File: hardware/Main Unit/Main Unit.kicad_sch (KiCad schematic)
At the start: 2 parts

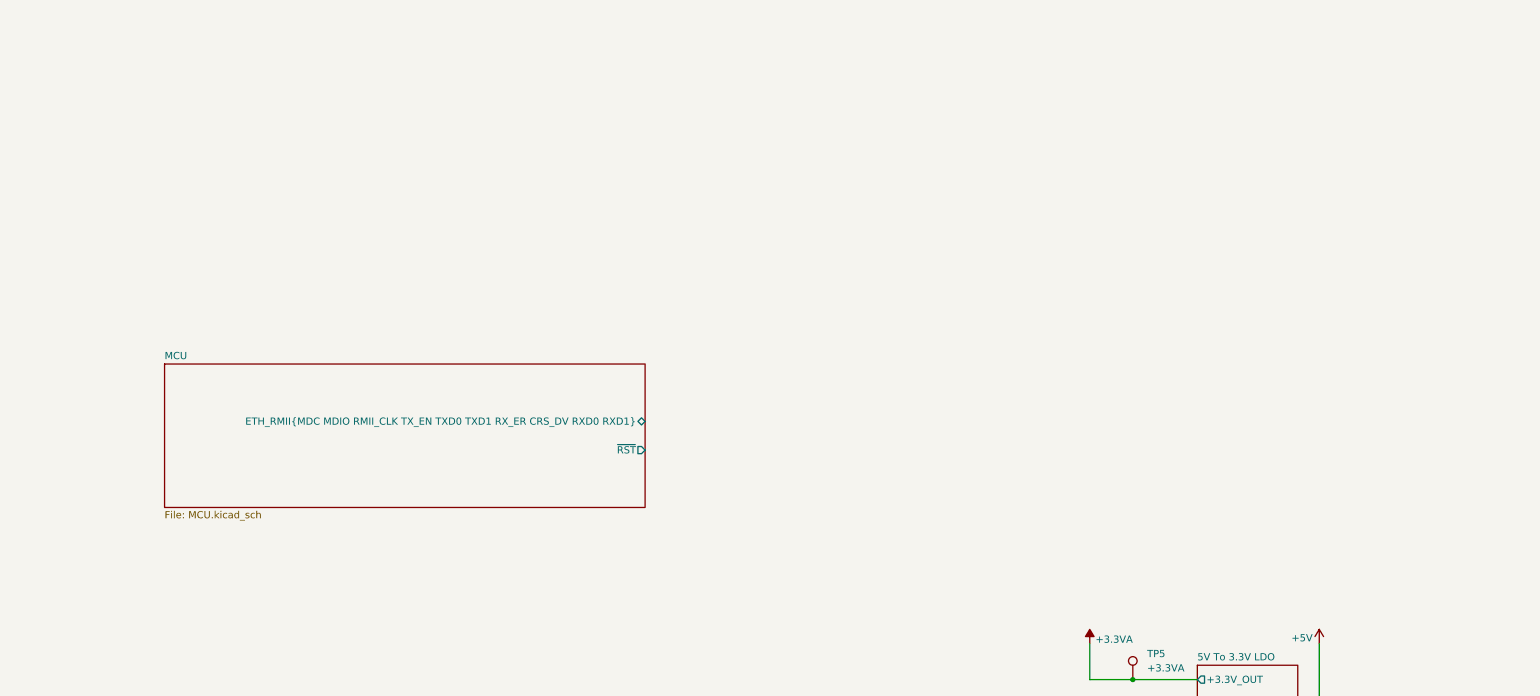
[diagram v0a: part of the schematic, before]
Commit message: Implement card connector schematic
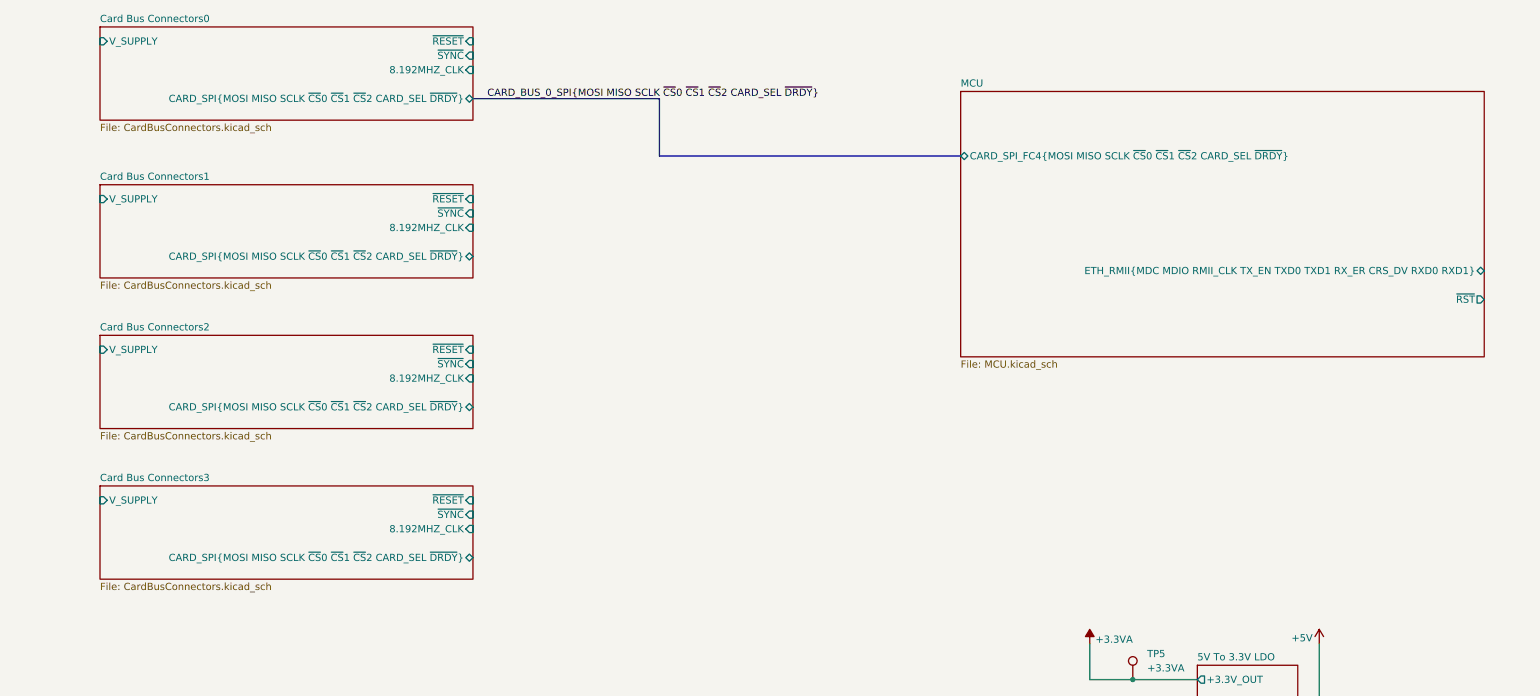
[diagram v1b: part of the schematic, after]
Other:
- added sheet Card Bus Connectors0 (CardBusConnectors.kicad_sch)
- added sheet Card Bus Connectors1 (CardBusConnectors.kicad_sch)
- added sheet Card Bus Connectors2 (CardBusConnectors.kicad_sch)
- added sheet Card Bus Connectors3 (CardBusConnectors.kicad_sch)
- sheet MCU ports: added CARD_SPI_FC4{MOSI MISO SCLK ~{CS}0 ~{CS}1 ~{CS}2 CARD_SEL ~{DRDY}}; removed none

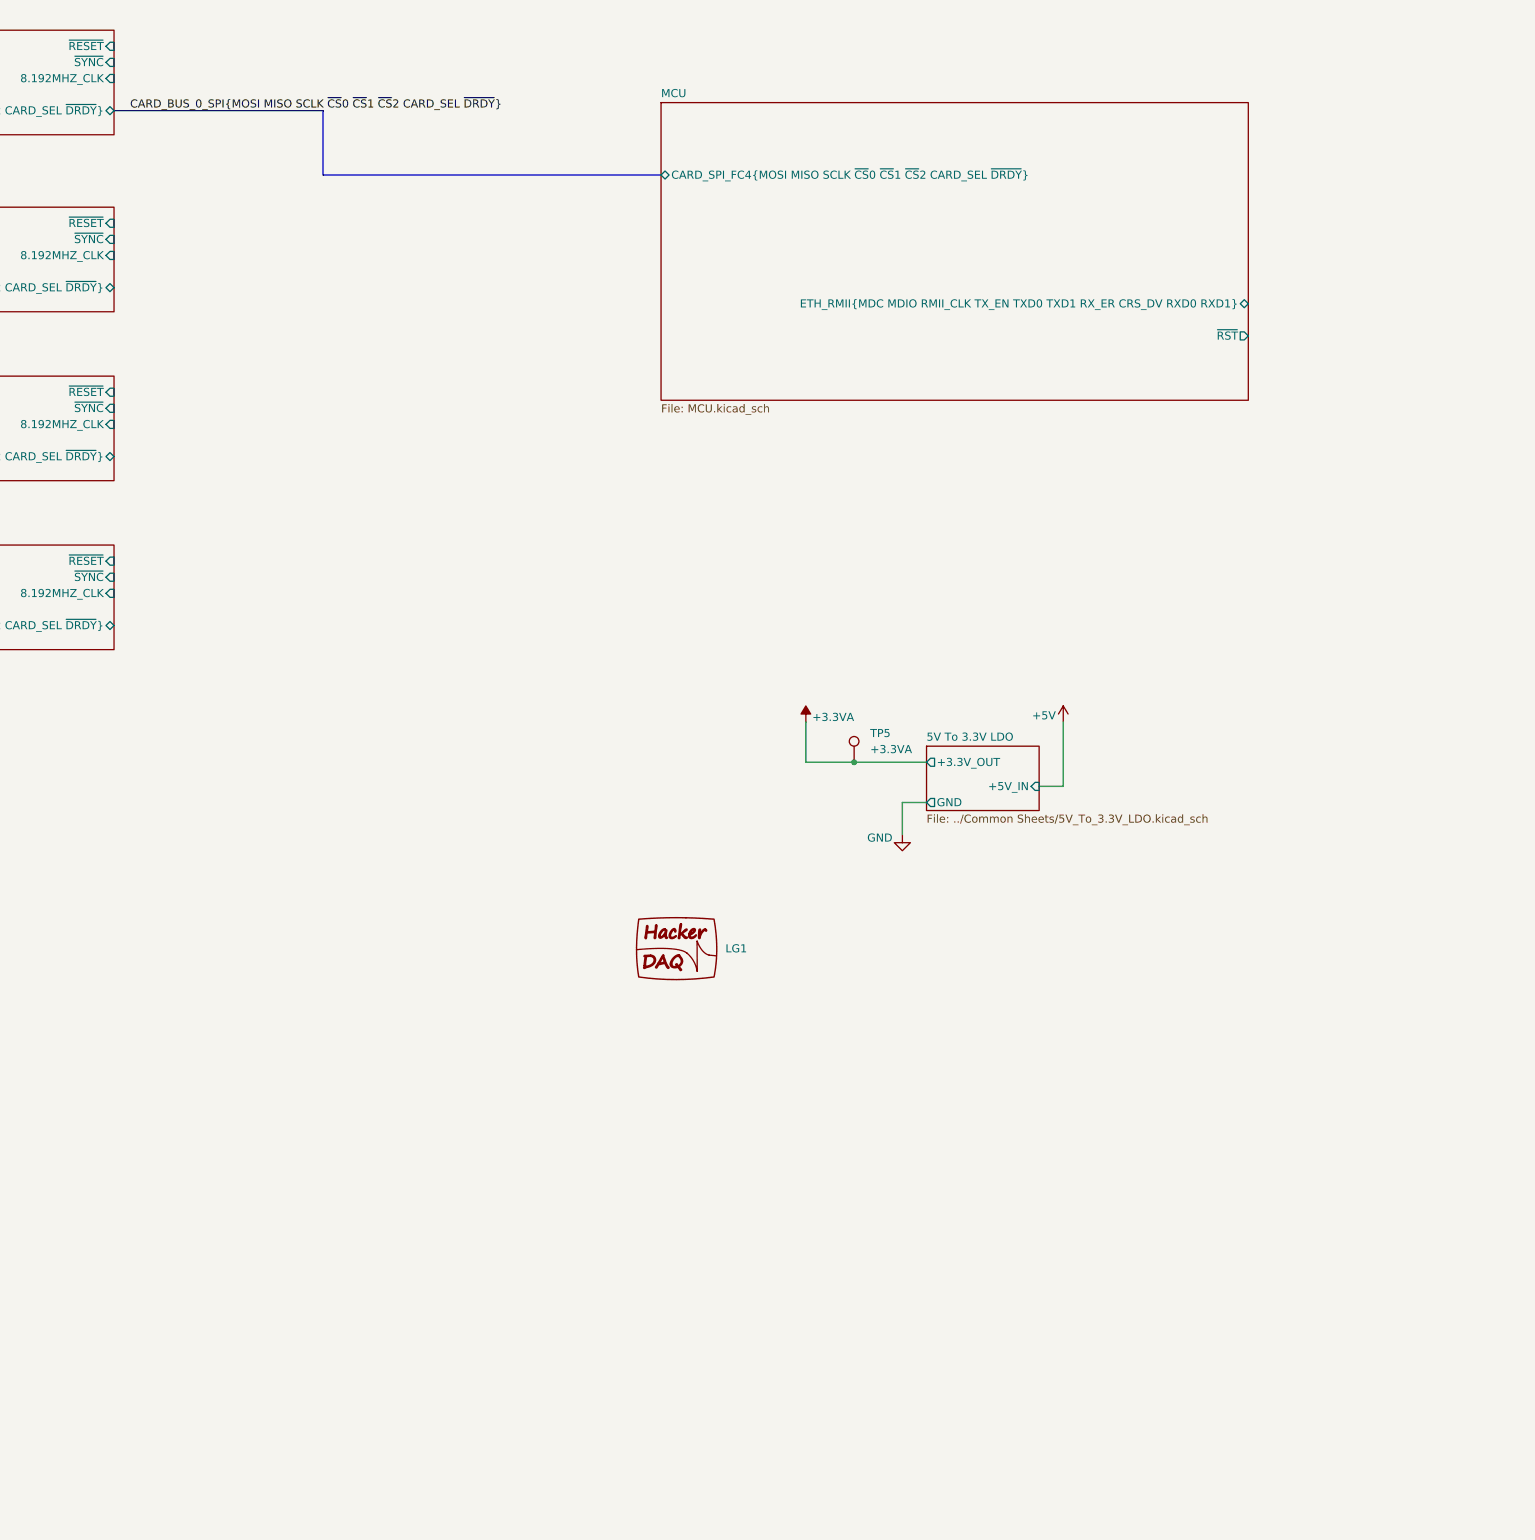
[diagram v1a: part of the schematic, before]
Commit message: Add MicroSD card, finish MCU symbol
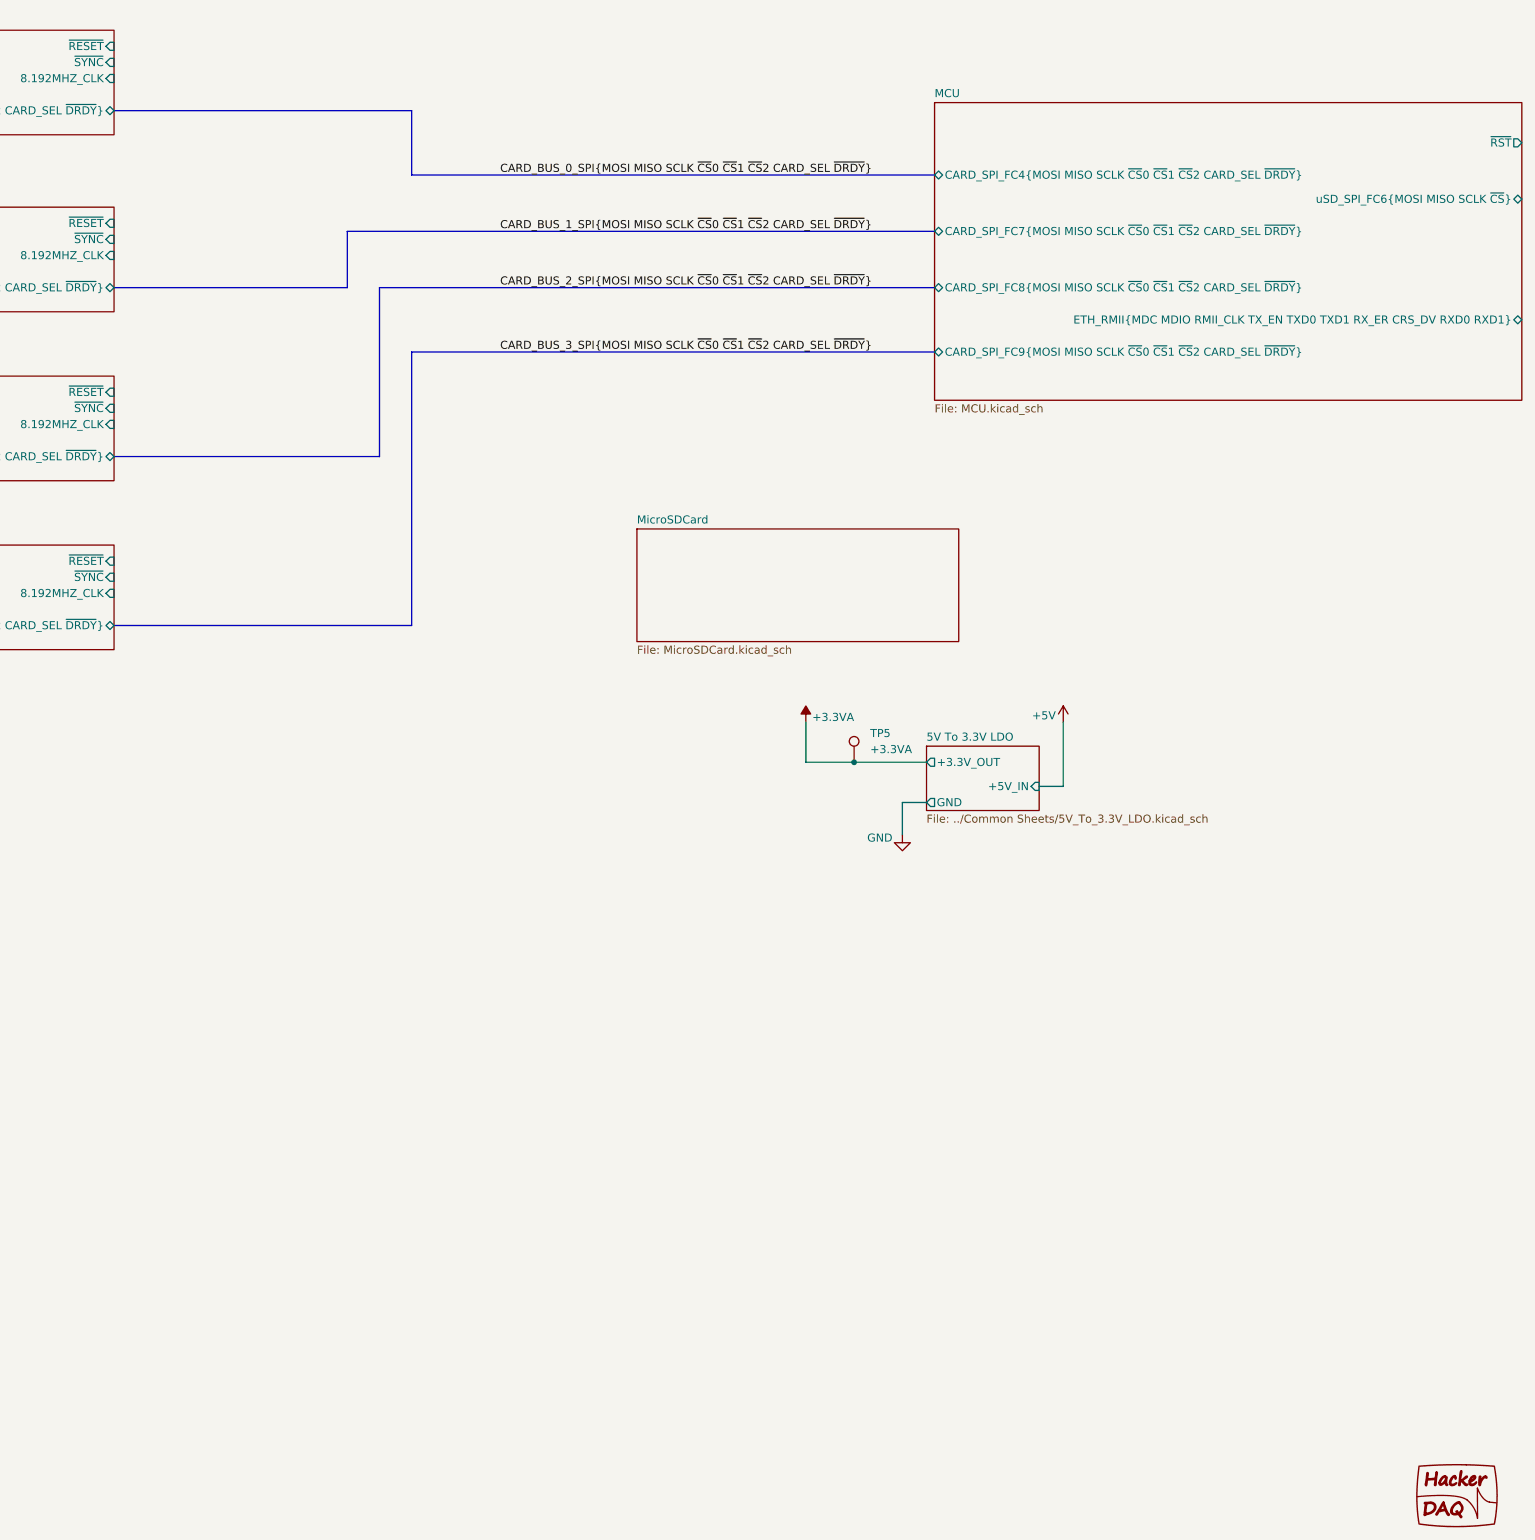
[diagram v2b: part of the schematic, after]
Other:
- added sheet MicroSDCard (MicroSDCard.kicad_sch)
- sheet MCU ports: added CARD_SPI_FC7{MOSI MISO SCLK ~{CS}0 ~{CS}1 ~{CS}2 CARD_SEL ~{DRDY}}, CARD_SPI_FC8{MOSI MISO SCLK ~{CS}0 ~{CS}1 ~{CS}2 CARD_SEL ~{DRDY}}, CARD_SPI_FC9{MOSI MISO SCLK ~{CS}0 ~{CS}1 ~{CS}2 CARD_SEL ~{DRDY}}, uSD_SPI_FC6{MOSI MISO SCLK ~{CS}}; removed none
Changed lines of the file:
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@@
 	(generator "eeschema")
 	(generator_version "9.0")
-	(paper "A4")
+	(paper "A3")
 	(junction
 		(at 213.36 144.78)
@@
 		(color 0 0 0 0)
 	)
+	(bus
+		(pts
+			(xy 138.43 69.85) (xy 226.06 69.85)
+		)
+		(stroke
+			(width 0)
+			(type default)
+		)
+	)
 	(wire
 		(pts
@@
 	(bus
 		(pts
-			(xy 129.54 52.07) (xy 129.54 41.91)
+			(xy 143.51 52.07) (xy 143.51 41.91)
 		)
 		(stroke
@@
 		)
 	)
+	(bus
+		(pts
+			(xy 133.35 60.96) (xy 133.35 69.85)
+		)
+		(stroke
+			(width 0)
+			(type default)
+		)
+	)
+	(bus
+		(pts
+			(xy 138.43 96.52) (xy 96.52 96.52)
+		)
+		(stroke
+			(width 0)
+			(type default)
+		)
+	)
+	(bus
+		(pts
+			(xy 143.51 123.19) (xy 96.52 123.19)
+		)
+		(stroke
+			(width 0)
+			(type default)
+		)
+	)
+	(bus
+		(pts
+			(xy 138.43 69.85) (xy 138.43 96.52)
+		)
+		(stroke
+			(width 0)
+			(type default)
+		)
+	)
+	(bus
+		(pts
+			(xy 143.51 80.01) (xy 143.51 123.19)
+		)
+		(stroke
+			(width 0)
+			(type default)
+		)
+	)
+	(bus
+		(pts
+			(xy 143.51 80.01) (xy 226.06 80.01)
+		)
+		(stroke
+			(width 0)
+			(type default)
+		)
+	)
 	(wire
 		(pts
@@
 	(bus
 		(pts
-			(xy 96.52 41.91) (xy 129.54 41.91)
+			(xy 96.52 41.91) (xy 143.51 41.91)
 		)
 		(stroke
@@
 	(bus
 		(pts
-			(xy 129.54 52.07) (xy 182.88 52.07)
+			(xy 143.51 52.07) (xy 226.06 52.07)
+		)
+		(stroke
+			(width 0)
+			(type default)
+		)
+	)
+	(bus
+		(pts
+			(xy 133.35 60.96) (xy 226.06 60.96)
+		)
+		(stroke
+			(width 0)
+			(type default)
+		)
+	)
+	(bus
+		(pts
+			(xy 133.35 69.85) (xy 96.52 69.85)
 		)
 		(stroke
@@
 	)
 	(label "CARD_BUS_0_SPI{MOSI MISO SCLK ~{CS}0 ~{CS}1 ~{CS}2 CARD_SEL ~{DRDY}}"
-		(at 99.06 41.91 0)
+		(at 157.48 52.07 0)
+		(effects
+			(font
+				(size 1.27 1.27)
+			)
+			(justify left bottom)
+		)
+	)
+	(label "CARD_BUS_2_SPI{MOSI MISO SCLK ~{CS}0 ~{CS}1 ~{CS}2 CARD_SEL ~{DRDY}}"
+		(at 157.48 69.85 0)
+		(effects
+			(font
+				(size 1.27 1.27)
+			)
+			(justify left bottom)
+		)
+	)
+	(label "CARD_BUS_3_SPI{MOSI MISO SCLK ~{CS}0 ~{CS}1 ~{CS}2 CARD_SEL ~{DRDY}}"
+		(at 157.48 80.01 0)
+		(effects
+			(font
+				(size 1.27 1.27)
+			)
+			(justify left bottom)
+		)
+	)
+	(label "CARD_BUS_1_SPI{MOSI MISO SCLK ~{CS}0 ~{CS}1 ~{CS}2 CARD_SEL ~{DRDY}}"
+		(at 157.48 60.96 0)
 		(effects
 			(font
@@
 	(symbol
 		(lib_id "Project Library:HackerDAQ_Logo")
-		(at 182.88 170.18 0)
+		(at 306.07 256.54 0)
 		(unit 1)
 		(exclude_from_sim no)
@@
 		(fields_autoplaced yes)
 		(property "Reference" "LG1"
-			(at 193.04 174.2016 0)
-			(effects
-				(font
-					(size 1.27 1.27)
-				)
-				(justify left)
+			(at 316.23 260.5616 0)
+			(effects
+				(font
+					(size 1.27 1.27)
+				)
+				(justify left)
+				(hide yes)
 			)
 		)
 		(property "Value" "~"
-			(at 182.88 170.18 0)
+			(at 306.07 256.54 0)
 			(effects
 				(font
@@
 		)
 		(property "Footprint" "Project Library:HackerDAQ Logo"
-			(at 194.056 165.1 0)
+			(at 317.246 251.46 0)
 			(effects
 				(font
@@
 		)
 		(property "Datasheet" ""
-			(at 182.88 170.18 0)
+			(at 306.07 256.54 0)
 			(effects
 				(font
@@
 		)
 		(property "Description" ""
-			(at 182.88 170.18 0)
+			(at 306.07 256.54 0)
 			(effects
 				(font
@@
 	)
 	(sheet
+		(at 179.07 107.95)
+		(size 50.8 17.78)
+		(exclude_from_sim no)
+		(in_bom yes)
+		(on_board yes)
+		(dnp no)
+		(fields_autoplaced yes)
+		(stroke
+			(width 0.1524)
+			(type solid)
+		)
+		(fill
+			(color 0 0 0 0.0000)
+		)
+		(property "Sheetname" "MicroSDCard"
+			(at 179.07 107.2384 0)
+			(effects
+				(font
+					(size 1.27 1.27)
+				)
+				(justify left bottom)
+			)
+		)
+		(property "Sheetfile" "MicroSDCard.kicad_sch"
+			(at 179.07 126.3146 0)
+			(effects
+				(font
+					(size 1.27 1.27)
+				)
+				(justify left top)
+			)
+		)
+		(instances
+			(project "Main Unit"
+				(path "/7d91f165-331a-4c48-9d02-ee2a0aa7e94a"
+					(page "8")
+				)
+			)
+		)
+	)
+	(sheet
 		(at 224.79 142.24)
 		(size 17.78 10.16)
@@
 	)
 	(sheet
-		(at 182.88 40.64)
+		(at 226.06 40.64)
 		(size 92.71 46.99)
 		(exclude_from_sim no)
@@
 		)
 		(property "Sheetname" "MCU"
-			(at 182.88 39.9284 0)
+			(at 226.06 39.9284 0)
 			(effects
 				(font
@@
 		)
 		(property "Sheetfile" "MCU.kicad_sch"
-			(at 182.88 88.2146 0)
+			(at 226.06 88.2146 0)
 			(effects
 				(font
@@
 		(pin "ETH_RMII{MDC MDIO RMII_CLK TX_EN TXD0 TXD1 RX_ER CRS_DV RXD0 RXD1}"
 			bidirectional
-			(at 275.59 72.39 0
+			(at 318.77 74.93 0
 			)
 			(effects
@@
 		)
 		(pin "~{RST}" output
-			(at 275.59 77.47 0)
+			(at 318.77 46.99 0)
 			(effects
 				(font
@@
 		(pin "CARD_SPI_FC4{MOSI MISO SCLK ~{CS}0 ~{CS}1 ~{CS}2 CARD_SEL ~{DRDY}}"
 			bidirectional
-			(at 182.88 52.07 180
-			)
-			(effects
-				(font
-					(size 1.27 1.27)
-				)
-				(justify left)
-			)
-		)
+			(at 226.06 52.07 180
+			)
+			(effects
+				(font
+					(size 1.27 1.27)
+				)
+				(justify left)
+			)
+		)
+		(pin "CARD_SPI_FC9{MOSI MISO SCLK ~{CS}0 ~{CS}1 ~{CS}2 CARD_SEL ~{DRDY}}"
+			bidirectional
+			(at 226.06 80.01 180
+			)
+			(effects
+				(font
+					(size 1.27 1.27)
+				)
+				(justify left)
+			)
+		)
+		(pin "CARD_SPI_FC8{MOSI MISO SCLK ~{CS}0 ~{CS}1 ~{CS}2 CARD_SEL ~{DRDY}}"
+			bidirectional
+			(at 226.06 69.85 180
+			)
+			(effects
+				(font
+					(size 1.27 1.27)
+				)
+				(justify left)
+			)
+		)
+		(pin "CARD_SPI_FC7{MOSI MISO SCLK ~{CS}0 ~{CS}1 ~{CS}2 CARD_SEL ~{DRDY}}"
+			bidirectional
+			(at 226.06 60.96 180
+			)
+			(effects
+				(font
+					(size 1.27 1.27)
+				)
+				(justify left)
+			)
+		)
+		(pin "uSD_SPI_FC6{MOSI MISO SCLK ~{CS}}" bidirectional
+			(at 318.77 55.88 0)
+			(effects
+				(font
+					(size 1.27 1.27)
+				)
+				(justify right)
+			)
+		)

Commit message: Implement Ethernet, start on voltage regulator
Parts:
- removed TP5: +3.3VA, TestPoint:TestPoint_THTPad_D2.5mm_Drill1.2mm, symbol Connector:TestPoint
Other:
- removed sheet 5V To 3.3V LDO
- added sheet DebugUSBUART (DebugUSBUART.kicad_sch)
- added sheet EthernetInterface (EthernetInterface.kicad_sch)
- added sheet SupplyTo3.3VRegulator (SupplyTo3.3VRegulator.kicad_sch)
- sheet MCU ports: added DBG_UART{MCU_TX MCU_RX}, ~{ETH_SPEED_LED}, ~{SD_CARD_EN}; removed none
- sheet MicroSDCard ports: added SPI{SCLK MOSI MISO ~{CS}}, ~{CARD_EN}; removed none
- note added: "Card Connectors"
- note added: "Ethernet"
- note added: "MCU"
- note added: "SD Card"

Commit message: Finish 3.3V regulator
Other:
- sheet Card Bus Connectors0 ports: added V_{SUPPLY}; removed V_SUPPLY
- sheet Card Bus Connectors1 ports: added V_{SUPPLY}; removed V_SUPPLY
- sheet Card Bus Connectors2 ports: added V_{SUPPLY}; removed V_SUPPLY
- sheet Card Bus Connectors3 ports: added V_{SUPPLY}; removed V_SUPPLY
- sheet MCU ports: added +3.3V_CUR_SENSE, +5V_CUR_SENSE; removed none
- sheet SupplyTo3.3VRegulator ports: added +3.3V, +3.3V_CUR_SENSE, PG, V_{SUPPLY}; removed none
